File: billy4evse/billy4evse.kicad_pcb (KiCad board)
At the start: 2 copper layers, 49.7 x 86.4 mm, 36 parts, among them J1 Conn_01x02, J10 Screw_Terminal_01x02, J2 Screw_Terminal_01x02, J3 Conn_02x06_Odd_Even, J4 Screw_Terminal_01x02, J5 AudioJack3, J6 AudioJack3, J7 USB_B_Micro, J8 AudioJack3, J9 Screw_Terminal_01x02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

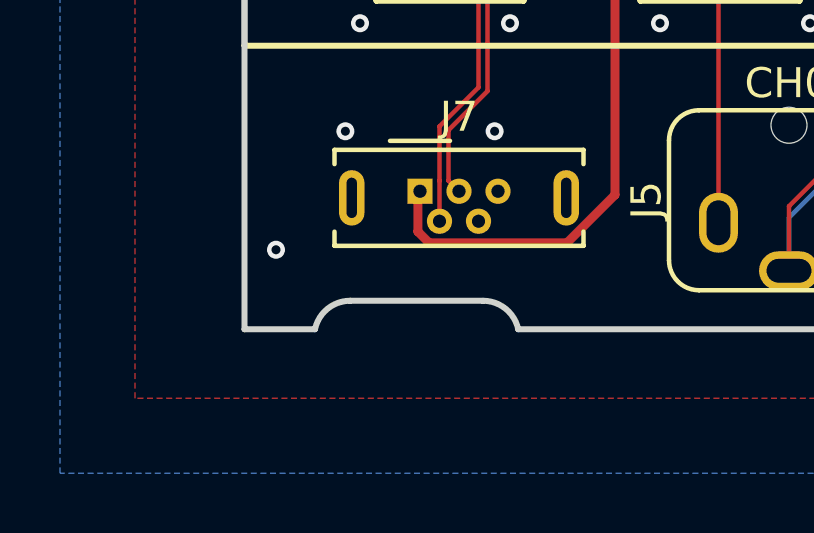
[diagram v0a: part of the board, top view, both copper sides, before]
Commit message: billy{sch, pcb}: Finish LCSC P/N list and fix bottom-left PCB notch
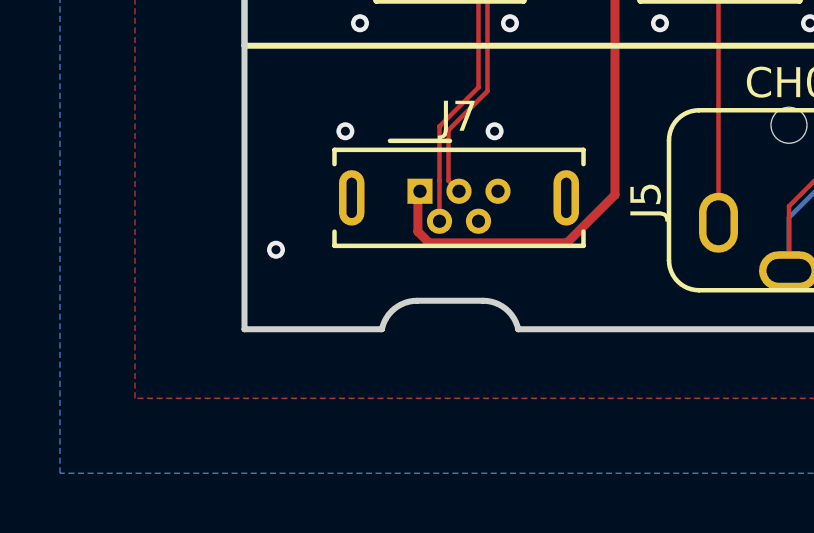
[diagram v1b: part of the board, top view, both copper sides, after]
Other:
- outline, holes or cut-outs redrawn
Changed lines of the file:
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@@
     (solder_mask_min_width 0.25)
     (aux_axis_origin 0 0)
-    (visible_elements FFFFFF7F)
+    (visible_elements 7FFFFFFF)
     (pcbplotparams
       (layerselection 0x010fc_ffffffff)
@@
   (gr_arc (start 120.7 71) (end 121.9 71) (angle -67.9756999) (layer Edge.Cuts) (width 0.2))
   (gr_line (start 121.15 114.1124) (end 121.15 135.2) (layer Edge.Cuts) (width 0.2))
-  (gr_line (start 124.673684 134.25) (end 129.1 134.25) (layer Edge.Cuts) (width 0.2))
+  (gr_line (start 126.903684 134.25) (end 129.1 134.25) (layer Edge.Cuts) (width 0.2))
   (gr_arc (start 171.3 113) (end 170.1 113.000021) (angle -67.975) (layer Edge.Cuts) (width 0.2))
-  (gr_arc (start 124.673684 135.45) (end 124.673684 134.25) (angle -77.97858788) (layer Edge.Cuts) (width 0.2))
+  (gr_arc (start 126.903684 135.45) (end 126.903684 134.25) (angle -77.97858788) (layer Edge.Cuts) (width 0.2))
   (gr_line (start 170.85 135.2) (end 170.85 114.1124) (layer Edge.Cuts) (width 0.2))
   (gr_arc (start 162.9 48.55) (end 161.726331 48.800007) (angle -77.975) (layer Edge.Cuts) (width 0.2))
@@
   (gr_arc (start 147.1 135.45) (end 148.273669 135.2) (angle -77.9753) (layer Edge.Cuts) (width 0.2))
   (gr_arc (start 165.1 48.55) (end 165.1 49.75) (angle -77.9753) (layer Edge.Cuts) (width 0.2))
-  (gr_line (start 121.15 135.2) (end 123.5 135.200067) (layer Edge.Cuts) (width 0.2))
+  (gr_line (start 121.15 135.2) (end 125.73 135.200067) (layer Edge.Cuts) (width 0.2))
   (gr_line (start 166.27 135.2) (end 170.85 135.2) (layer Edge.Cuts) (width 0.2))
   (gr_line (start 121.9 71) (end 121.9 113) (layer Edge.Cuts) (width 0.2))
